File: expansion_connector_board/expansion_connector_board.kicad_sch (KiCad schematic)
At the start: 17 parts, among them J1 Conn_01x04, J12 Conn_02x17_Top_Bottom, J13 Conn_01x04, J14 Conn_02x17_Top_Bottom, J19 MEGA65 R4+ Analog Audio Header, J2 ESP32 JTAG+UART (TE0790), J3 ESP32 UART Breakout, J4 ESP32 Bootstraps, J5 ESP32 Sensor, J6 ESP32/Peripheral UART Interfa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, J7 Conn_01x04, U1 ESP32-WROOM-32D

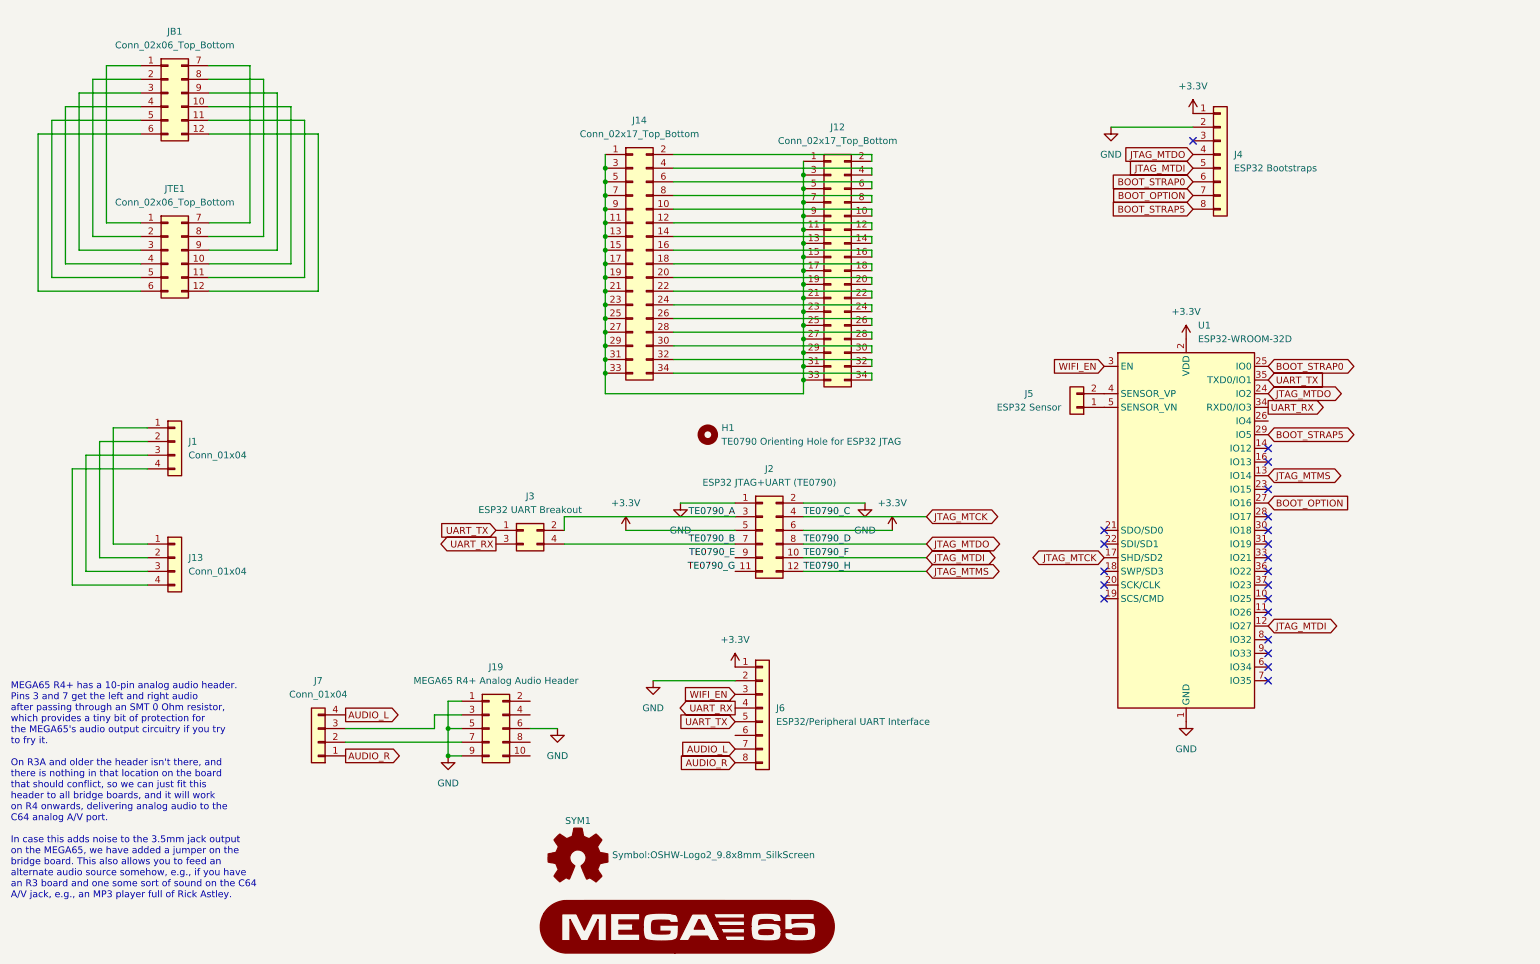
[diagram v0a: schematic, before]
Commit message: remove ESP32 and replace with PicoPi W and JTAG hijack for core loader
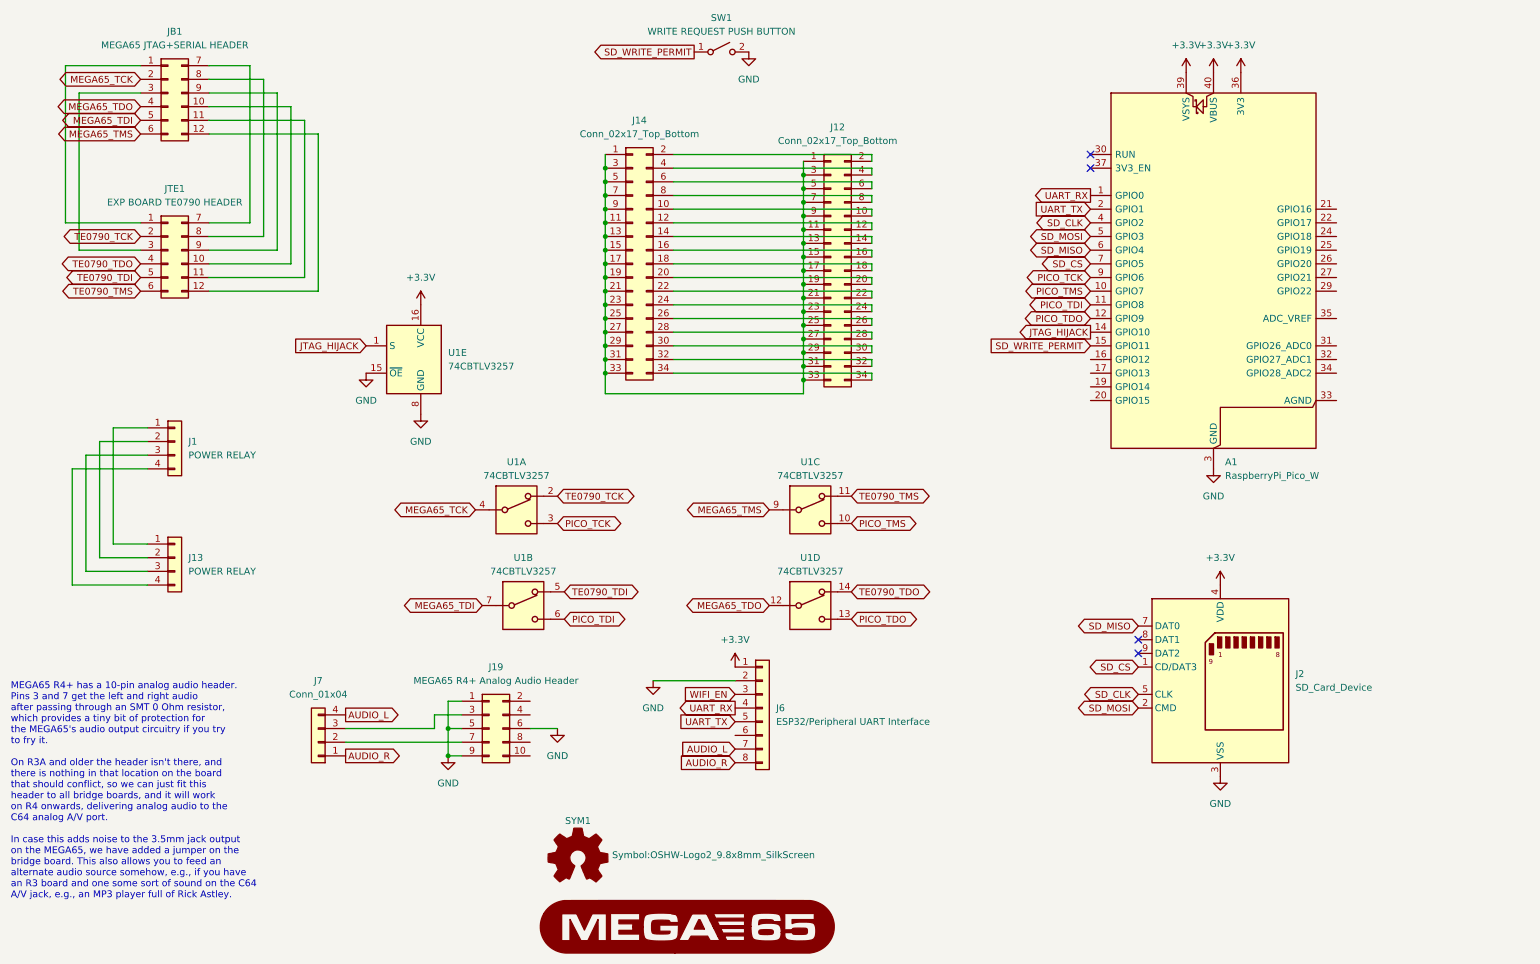
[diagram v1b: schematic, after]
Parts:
- removed H1: TE0790 Orienting Hole for ESP32 JTAG, MountingHole:MountingHole_3.2mm_M3_Pad, symbol Mechanical:MountingHole
- removed J2: ESP32 JTAG+UART (TE0790), Connector_PinHeader_2.54mm:PinHeader_2x06_P2.54mm_Vertical, symbol Connector_Generic:Conn_02x06_Odd_Even
- removed J3: ESP32 UART Breakout, Connector_PinHeader_2.54mm:PinHeader_2x02_P2.54mm_Vertical, symbol Connector_Generic:Conn_02x02_Odd_Even
- removed J4: ESP32 Bootstraps, Connector_PinHeader_2.54mm:PinHeader_1x08_P2.54mm_Vertical, symbol Connector_Generic:Conn_01x08
- removed J5: ESP32 Sensor, Connector_PinHeader_2.54mm:PinHeader_1x02_P2.54mm_Horizontal, symbol Connector_Generic:Conn_01x02
- removed U1: ESP32-WROOM-32D, RF_Module:ESP32-WROOM-32D, symbol RF_Module:ESP32-WROOM-32D
- added A1: RaspberryPi_Pico_W, Module:RaspberryPi_Pico_W_SMD_HandSolder, symbol MCU_Module:RaspberryPi_Pico_W
- added J2: SD_Card_Device, Connector_Card:SD_Card_Device_16mm_SlotDepth, symbol Connector:SD_Card_Device
- added SW1: WRITE REQUEST PUSH BUTTON, symbol Switch:SW_SPST
- added U1: 74CBTLV3257, Package_SO:SOIC-16_3.9x9.9mm_P1.27mm, symbol 74xx:74CBTLV3257
- J1, J13: value Conn_01x04 -> POWER RELAY
- JB1: value Conn_02x06_Top_Bottom -> MEGA65 JTAG+SERIAL HEADER
- JTE1: value Conn_02x06_Top_Bottom -> EXP BOARD TE0790 HEADER
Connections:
- net +3.3V: now also A1.36 (3V3), A1.39 (VSYS), A1.40 (VBUS), J2.4 (VDD), U1.16 (VCC)
- net GND: now also A1.13 (GND), A1.18 (GND), A1.23 (GND), A1.28 (GND), A1.3 (GND), A1.38 (GND), A1.8 (GND), J2.3 (VSS), J2.6 (VSS), SW1.2 (B), U1.15 (~{OE}), U1.8 (GND)
- net UART_RX: now also A1.1 (GPIO0)
- net UART_TX: now also A1.2 (GPIO1)
- net MEGA65_TCK: now reaches JB1.2 (Pin_2)
- net MEGA65_TCK: now also U1.4; no longer JTE1.2 (Pin_2)
- net MEGA65_TDO: now reaches JB1.4 (Pin_4)
- net MEGA65_TDO: now also U1.12; no longer JTE1.4 (Pin_4)
- net MEGA65_TDI: now reaches JB1.5 (Pin_5)
- net MEGA65_TDI: now also U1.7; no longer JTE1.5 (Pin_5)
- net MEGA65_TMS: now reaches JB1.6 (Pin_6)
- net MEGA65_TMS: now also U1.9; no longer JTE1.6 (Pin_6)
- new net JTAG_HIJACK: A1.14 (GPIO10), U1.1 (S)
- new net PICO_TCK: A1.9 (GPIO6), U1.3
- new net PICO_TDI: A1.11 (GPIO8), U1.6
- new net PICO_TDO: A1.12 (GPIO9), U1.13
- new net PICO_TMS: A1.10 (GPIO7), U1.10
- new net SD_CLK: A1.4 (GPIO2), J2.5 (CLK)
- new net SD_CS: A1.7 (GPIO5), J2.1 (CD/DAT3)
- new net SD_MISO: A1.6 (GPIO4), J2.7 (DAT0)
- new net SD_MOSI: A1.5 (GPIO3), J2.2 (CMD)
- new net SD_WRITE_PERMIT: A1.15 (GPIO11), SW1.1 (A)
- new net TE0790_TCK: JTE1.2 (Pin_2), U1.2
- new net TE0790_TDI: JTE1.5 (Pin_5), U1.5
- new net TE0790_TDO: JTE1.4 (Pin_4), U1.14
- new net TE0790_TMS: JTE1.6 (Pin_6), U1.11
- no-connect marks 21 -> 4

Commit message: rework bridge board for Pico Pi instead of ESP32
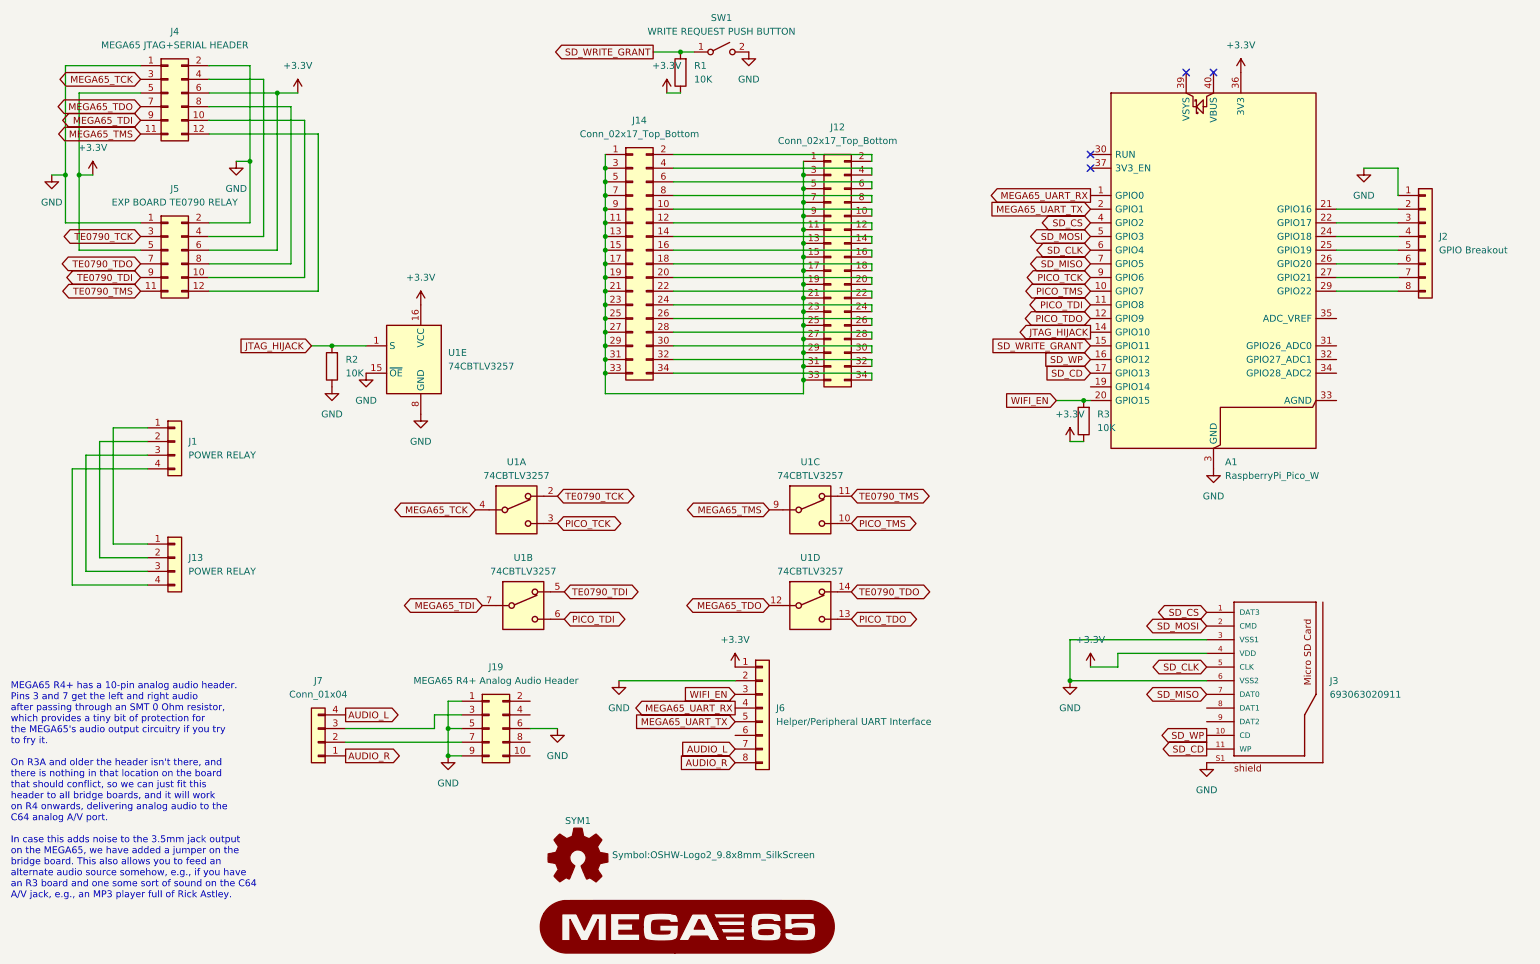
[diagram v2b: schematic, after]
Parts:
- removed J2: SD_Card_Device, Connector_Card:SD_Card_Device_16mm_SlotDepth, symbol Connector:SD_Card_Device
- removed JB1: MEGA65 JTAG+SERIAL HEADER, Connector_PinHeader_2.54mm:PinHeader_2x06_P2.54mm_Vertical, symbol Connector_Generic:Conn_02x06_Top_Bottom
- removed JTE1: EXP BOARD TE0790 HEADER, Connector_PinHeader_2.54mm:PinHeader_2x06_P2.54mm_Vertical, symbol Connector_Generic:Conn_02x06_Top_Bottom
- added J2: GPIO Breakout, Connector_PinHeader_2.54mm:PinHeader_1x08_P2.54mm_Vertical, symbol Connector_Generic:Conn_01x08
- added J3: 693063020911, snapeda:693063020911, symbol snapeda:693063020911
- added J4: MEGA65 JTAG+SERIAL HEADER, Connector_PinHeader_2.54mm:PinHeader_2x06_P2.54mm_Vertical, symbol Connector_Generic:Conn_02x06_Odd_Even
- added J5: EXP BOARD TE0790 RELAY, Connector_PinHeader_2.54mm:PinHeader_2x06_P2.54mm_Vertical, symbol Connector_Generic:Conn_02x06_Odd_Even
- added R1, R2, R3: 10K, Resistor_THT:R_Axial_DIN0207_L6.3mm_D2.5mm_P10.16mm_Horizontal, symbol Device:R
- J6: value ESP32/Peripheral UART Interface -> Helper/Peripheral UART Interface
- SW1: footprint (none) -> snapeda:TE_2-1825027-0
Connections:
- net +3.3V: now also J3.4 (VDD), J4.5 (Pin_5), J4.6 (Pin_6), J5.5 (Pin_5), J5.6 (Pin_6), R1.1, R3.1; no longer A1.39 (VSYS), A1.40 (VBUS)
- net GND: now also J2.1 (Pin_1), J3.3 (VSS1), J3.6 (VSS2), J3.S1, J3.S2, J3.S3, J3.S4, J4.1 (Pin_1), J4.2 (Pin_2), J5.1 (Pin_1), J5.2 (Pin_2), R2.1
- net JTAG_HIJACK: now also R2.2
- net MEGA65_TCK: now also J4.3 (Pin_3)
- net MEGA65_TDI: now also J4.9 (Pin_9)
- net MEGA65_TDO: now also J4.7 (Pin_7)
- net MEGA65_TMS: now also J4.11 (Pin_11)
- net SD_CLK: now also A1.6 (GPIO4), J3.5 (CLK); no longer A1.4 (GPIO2)
- net SD_CS: now also A1.4 (GPIO2), J3.1 (DAT3); no longer A1.7 (GPIO5)
- net SD_MISO: now also A1.7 (GPIO5), J3.7 (DAT0); no longer A1.6 (GPIO4)
- net SD_MOSI: now also J3.2 (CMD)
- net TE0790_TCK: now also J5.3 (Pin_3)
- net TE0790_TDI: now also J5.9 (Pin_9)
- net TE0790_TDO: now also J5.7 (Pin_7)
- net TE0790_TMS: now also J5.11 (Pin_11)
- net WIFI_EN: now also A1.20 (GPIO15), R3.2
- net SD_WP: now reaches A1.16 (GPIO12)
- net SD_WP: now also J3.10 (CD)
- net SD_CD: now reaches A1.17 (GPIO13)
- net SD_CD: now also J3.11 (WP)
- net at A1.21 (GPIO16): now also J2.2 (Pin_2)
- net at A1.22 (GPIO17): now also J2.3 (Pin_3)
- net at A1.24 (GPIO18): now also J2.4 (Pin_4)
- net at A1.25 (GPIO19): now also J2.5 (Pin_5)
- net at A1.26 (GPIO20): now also J2.6 (Pin_6)
- net at A1.27 (GPIO21): now also J2.7 (Pin_7)
- net at A1.29 (GPIO22): now also J2.8 (Pin_8)
- net SD_WRITE_PERMIT renamed SD_WRITE_GRANT
- net SD_WRITE_GRANT: now also R1.2
- net UART_RX renamed MEGA65_UART_RX
- net UART_TX renamed MEGA65_UART_TX
- new net: J4.10 (Pin_10), J5.10 (Pin_10)
- new net: J4.12 (Pin_12), J5.12 (Pin_12)
- new net: J4.4 (Pin_4), J5.4 (Pin_4)
- new net: J4.8 (Pin_8), J5.8 (Pin_8)

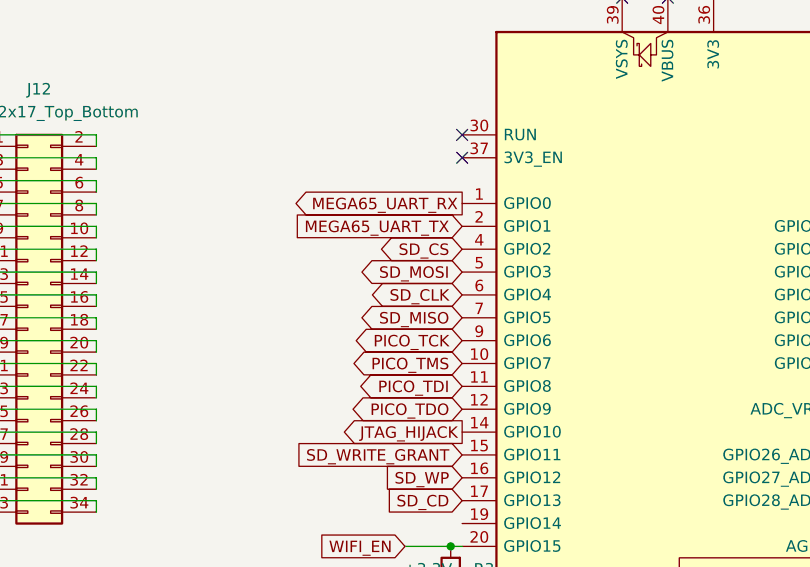
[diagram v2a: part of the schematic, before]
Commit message: use hardware SPI pinout
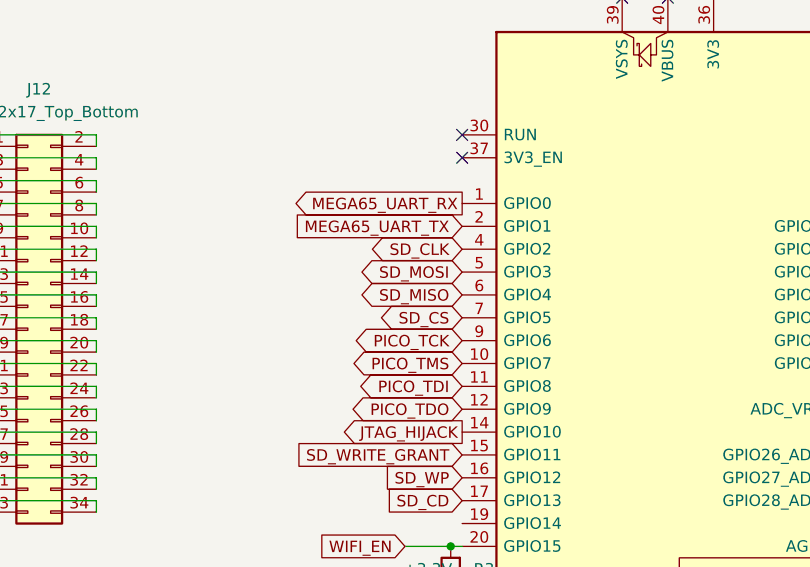
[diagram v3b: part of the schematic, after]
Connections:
- net SD_CLK: now also A1.4 (GPIO2); no longer A1.6 (GPIO4)
- net SD_CS: now also A1.7 (GPIO5); no longer A1.4 (GPIO2)
- net SD_MISO: now also A1.6 (GPIO4); no longer A1.7 (GPIO5)
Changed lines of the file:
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@@
 	(global_label "SD_CS"
 		(shape bidirectional)
-		(at 218.44 57.15 180)
-		(fields_autoplaced yes)
-		(effects
-			(font
-				(size 1.27 1.27)
-			)
-			(justify right)
-		)
-		(property "Intersheetrefs" "${INTERSHEET_REFS}"
-			(at 208.4169 57.15 0)
+		(at 218.44 64.77 180)
+		(fields_autoplaced yes)
+		(effects
+			(font
+				(size 1.27 1.27)
+			)
+			(justify right)
+		)
+		(property "Intersheetrefs" "${INTERSHEET_REFS}"
+			(at 208.4169 64.77 0)
 			(effects
 				(font
@@
 	(global_label "SD_CLK"
 		(shape bidirectional)
-		(at 218.44 62.23 180)
-		(fields_autoplaced yes)
-		(effects
-			(font
-				(size 1.27 1.27)
-			)
-			(justify right)
-		)
-		(property "Intersheetrefs" "${INTERSHEET_REFS}"
-			(at 207.3283 62.23 0)
+		(at 218.44 57.15 180)
+		(fields_autoplaced yes)
+		(effects
+			(font
+				(size 1.27 1.27)
+			)
+			(justify right)
+		)
+		(property "Intersheetrefs" "${INTERSHEET_REFS}"
+			(at 207.3283 57.15 0)
 			(effects
 				(font
@@
 	(global_label "SD_MISO"
 		(shape bidirectional)
-		(at 218.44 64.77 180)
-		(fields_autoplaced yes)
-		(effects
-			(font
-				(size 1.27 1.27)
-			)
-			(justify right)
-		)
-		(property "Intersheetrefs" "${INTERSHEET_REFS}"
-			(at 206.3002 64.77 0)
-			(effects
-				(font
+		(at 218.44 62.23 180)
+		(fields_autoplaced yes)
+		(effects
+			(font
+				(size 1.27 1.27)
+			)
+			(justify right)
+		)
+		(property "Intersheetrefs" "${INTERSHEET_REFS}"
+			(at 206.3002 62.23 0)
+			(effects
+				(font

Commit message: protect 3.3v from MEGA65 into Pico Pi and generl tidying
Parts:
- added D1: 1N5819, Diode_THT:D_DO-41_SOD81_P10.16mm_Horizontal, symbol Diode:1N5819
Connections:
- net +3.3V: no longer J4.5 (Pin_5), J4.6 (Pin_6), J5.5 (Pin_5), J5.6 (Pin_6), J6.1 (Pin_1), U1.16 (VCC)
- net at A1.39 (VSYS): now also D1.1 (K)
- new net MEGA6_3V3: D1.2 (A), J4.5 (Pin_5), J4.6 (Pin_6), J5.5 (Pin_5), J5.6 (Pin_6), J6.1 (Pin_1), U1.16 (VCC)
- no-connect marks 4 -> 3
